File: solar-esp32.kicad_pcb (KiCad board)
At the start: 2 copper layers, 25.4 x 25.4 mm, 34 parts, among them J1 Solar, J2 BAT+, J3 BAT-, J4 ESP32, Q1 DMP1045U-7, Q2 SSM3J332RLF, U1 CN3801, U2 NCP302HSN30

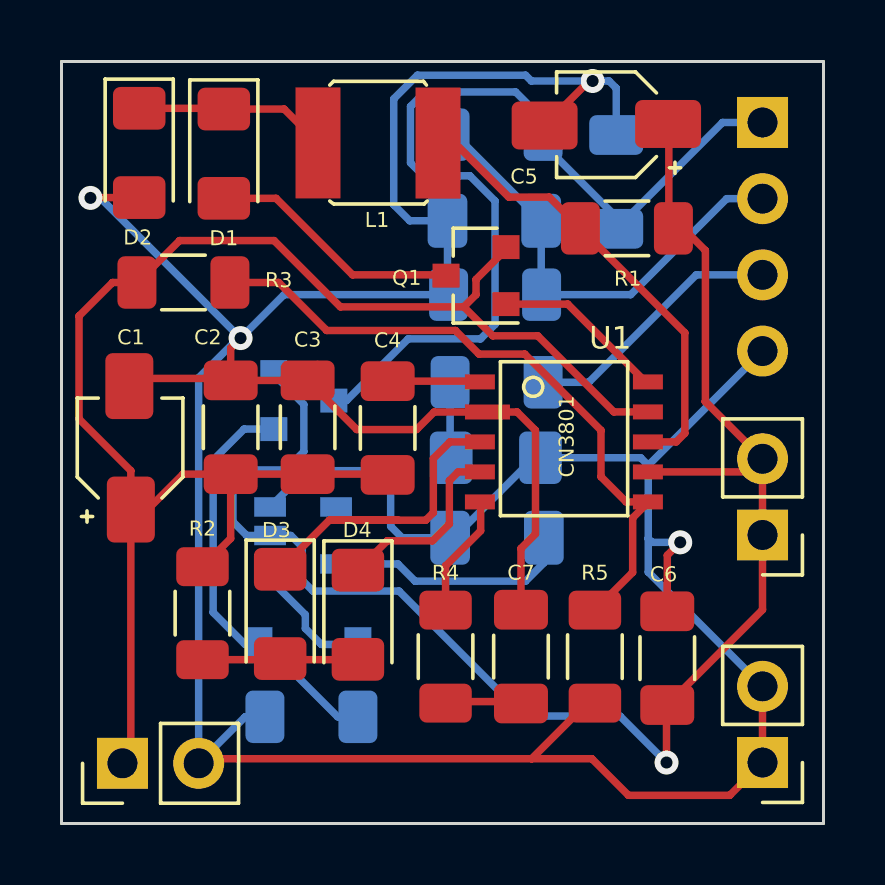
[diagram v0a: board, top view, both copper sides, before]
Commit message: Replaced active-high supervisor and p-channel mosfet with an active-low supervisor connected to EN (enable) pin on ESP32.
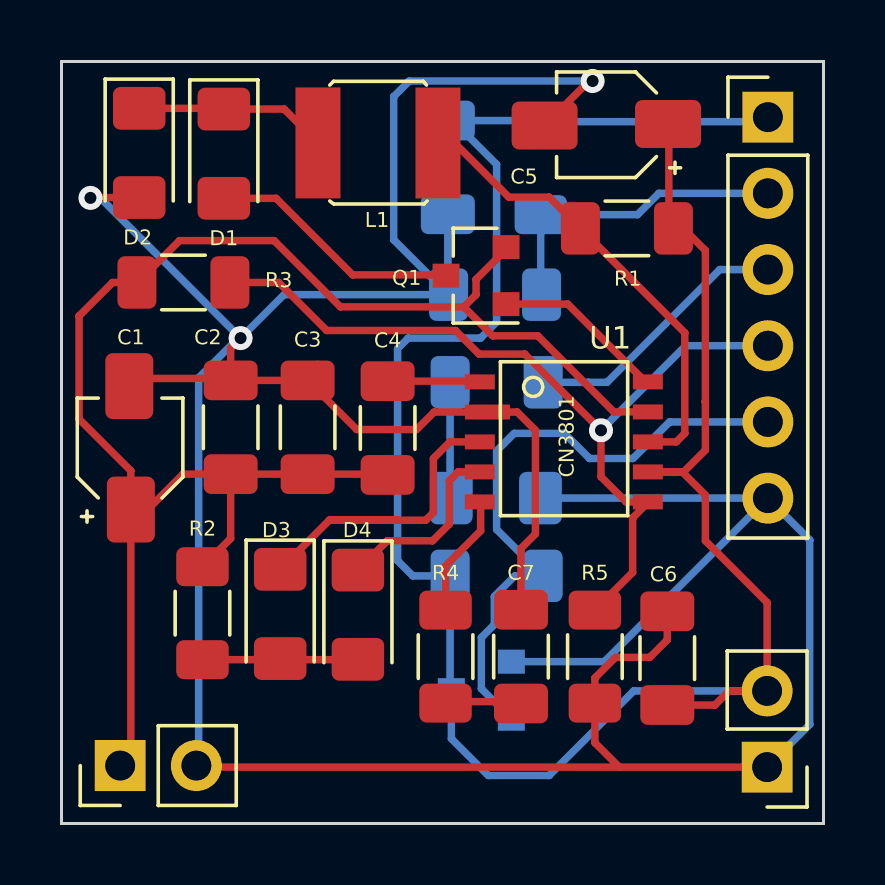
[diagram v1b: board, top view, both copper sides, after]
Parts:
- removed the C8 at (139.0, 87.6)
- removed C9: 100nF, Capacitor_SMD:C_1206_3216Metric_Pad1.33x1.80mm_HandSolder
- removed D5: D_Zener, Diode_SMD:D_SOD-123
- removed J3: BAT-, Connector_PinHeader_2.54mm:PinHeader_1x02_P2.54mm_Vertical
- removed Q2: SSM3J332RLF, Package_TO_SOT_SMD:SOT-23
- removed R6: 10k, Resistor_SMD:R_1206_3216Metric_Pad1.30x1.75mm_HandSolder
- added R10: 100k, Resistor_SMD:R_1206_3216Metric_Pad1.30x1.75mm_HandSolder, B.Cu at (139.0, 88.9)
- J2: value BAT+ -> BAT
- J4: footprint Connector_PinHeader_2.54mm:PinHeader_1x04_P2.54mm_Vertical -> Connector_PinHeader_2.54mm:PinHeader_1x06_P2.54mm_Vertical; moved to F.Cu
- U2: value NCP302HSN30 -> APX803L; footprint Package_TO_SOT_SMD:SOT-23-5 -> Package_TO_SOT_SMD:SOT-23
- moved U2 7.87 mm to (138.5, 92.7), turned to 180 degrees
- moved J2 7.74 mm to (148.0, 95.3)
- moved C8 5.63 mm to (137.3, 75.3), turned to 270 degrees
- moved R9 1.85 mm to (140.4, 75.3), turned to 270 degrees
- moved D6 1.35 mm to (138.9, 86.3)
- moved J4 0.25 mm to (148.0, 73.6), turned to 0 degrees
- moved J1 0.11 mm to (126.4, 95.2)
- renumbered C10 to C8
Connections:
- C8 pad 1: /ESP-LOAD -> /BAT+
- J2 pad 1: /BAT+ -> /GND
- J4 pad 1: /ESP-LOAD -> /BAT+
- J4 pad 4: /GND -> /MPPT
- R9 pad 1: /ESP-LOAD -> /BAT+
- U2 pad 1: Net-(D5-Pad1) -> /GND
- U2 pad 2: /BAT+ -> /EN
- U2 pad 3: /GND -> /BAT+
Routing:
- net /ESP-LOAD: track 31.8 -> 0.00 mm
- net /EN: track 0.00 -> 22.4 mm
- net /BAT+: track 53.6 -> 76.0 mm, vias 1 -> 0
- net /LVCO: track 13.8 -> 0.00 mm
- net /Cd: track 8.26 -> 0.00 mm
- net /GND: track 137.0 -> 129.1 mm, vias 4 -> 3
- net /MPPT: track 22.3 -> 29.0 mm, vias 0 -> 1
- net /ADC: track 16.2 -> 10.6 mm
- net Net-(D5-Pad1): track 4.50 -> 0.00 mm
- net /ESP-LED2: track 3.50 -> 4.85 mm
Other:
- board text added: "(c) 2021 dushin.net"
- board text added: "+"
- board text added: "+3.3v"
- board text added: "-"
- board text added: "Apache License 2.0"
- board text added: "BAT"
- board text added: "Solar in"
- board text added: "en"
- board text added: "gnd"
- board text added: "led"
- board text added: "solar-esp32"
- board text added: "v0.1.0"
- board text added: "vbat"
- board text added: "vsol"
- board text removed: "+3.3v ADC LED GND"
- board text removed: "+6v"
- board text removed: ".01"
- board text removed: "0xFD02"
- board text removed: "BAT+"
- board text removed: "BAT-"
- board text removed: "GND"
- board text removed: "Solar Panel"

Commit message: Changed to BSD 2.0 license, and added OpenHardware logo
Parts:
- added REF**: OSHW-Logo2_7.3x6mm_SilkScreen, Symbol:OSHW-Logo2_7.3x6mm_SilkScreen, B.Cu at (128.1, 86.1)
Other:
- board text added: "BSD License 2.0"
- board text removed: "Apache License 2.0"

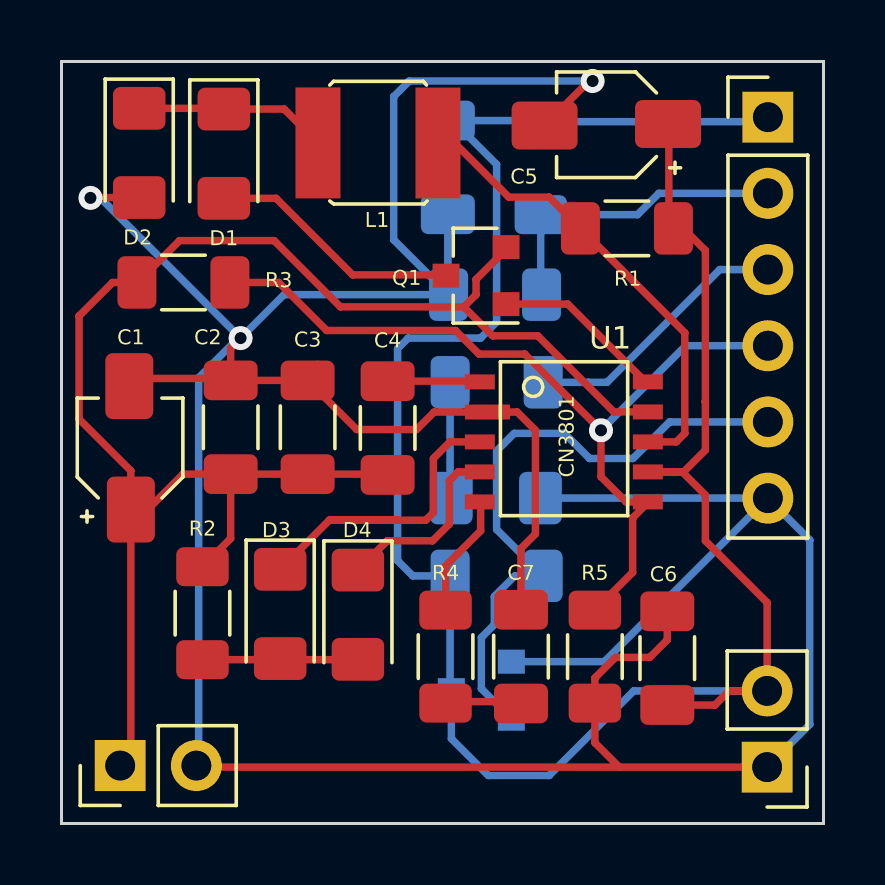
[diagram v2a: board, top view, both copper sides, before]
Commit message: Added 100uF capacitor near active-low supervisor.
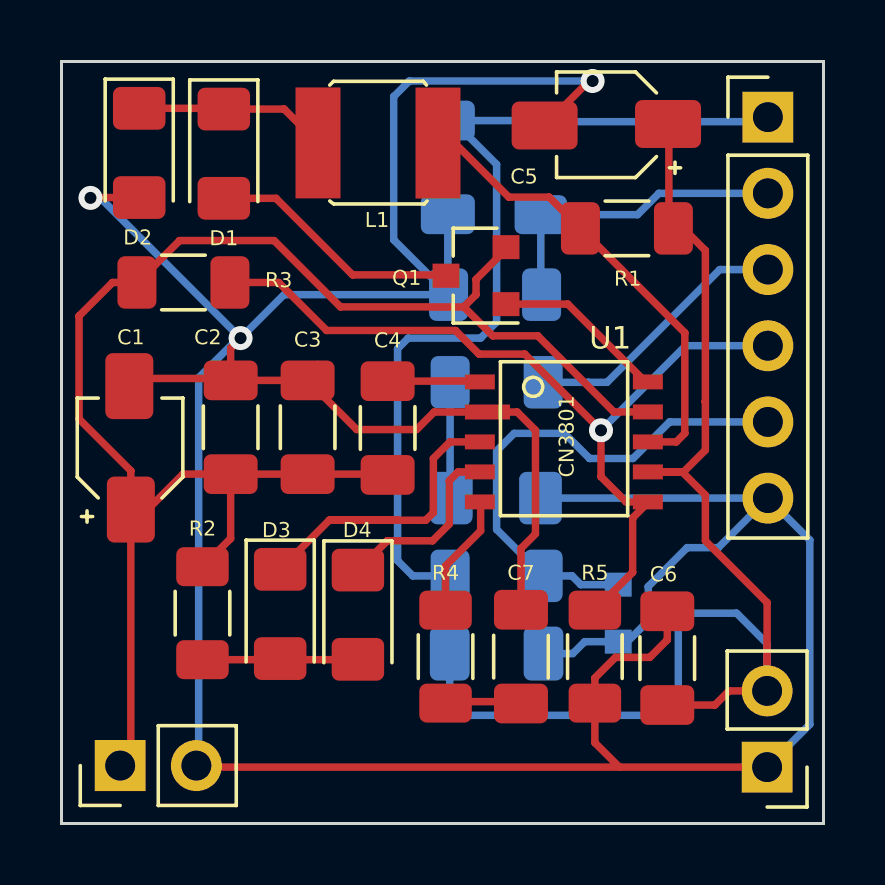
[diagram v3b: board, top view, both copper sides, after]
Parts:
- added C9: 100uF, Capacitor_SMD:C_1206_3216Metric_Pad1.33x1.80mm_HandSolder, B.Cu at (139.0, 91.5)
- moved U2 6.13 mm to (144.0, 90.1), turned to 0 degrees
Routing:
- net /EN: track 22.4 -> 18.5 mm
- net /BAT+: track 76.0 -> 77.7 mm
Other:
- board text added: "EN"
- board text added: "GND"
- board text added: "LED"
- board text added: "vBAT"
- board text added: "vSOL"
- board text removed: "en"
- board text removed: "gnd"
- board text removed: "led"
- board text removed: "vbat"
- board text removed: "vsol"
